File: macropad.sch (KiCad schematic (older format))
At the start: 36 parts, among them J1 USB_C_Receptacle_USB2.0, J2 TC2050-IDC, J3 CONN_LCD, U1 XC6206P332MR, U2 USBLC6-2SC6, U3 STM32F303RCTx, Y1 32MHz

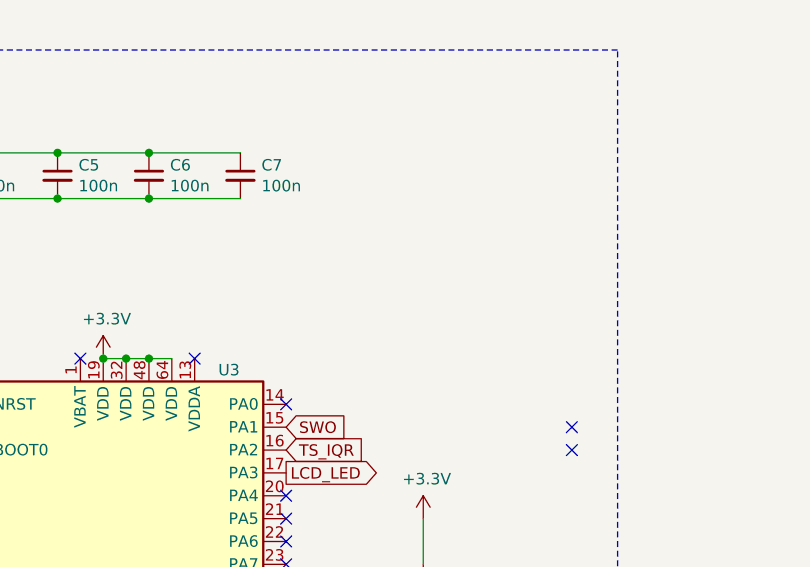
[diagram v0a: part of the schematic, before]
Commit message: Added known issues list to readme and a todo to the schematic
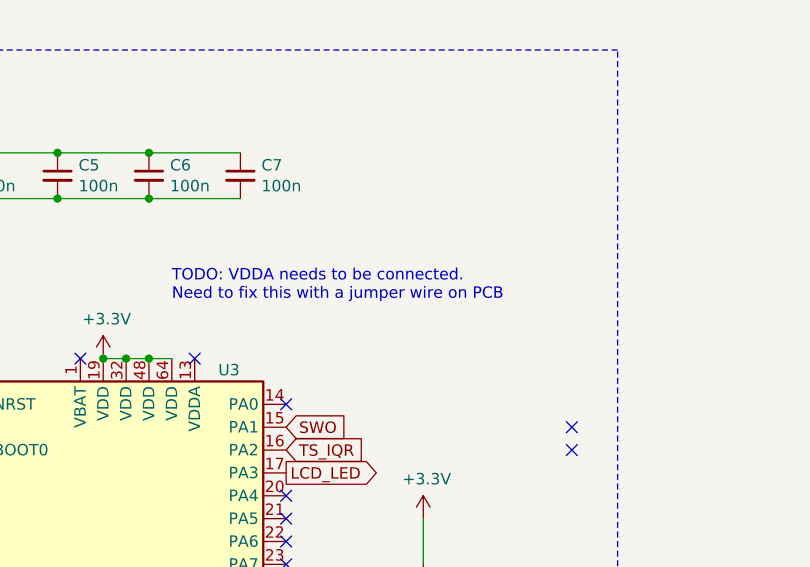
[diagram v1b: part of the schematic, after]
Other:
- note added: "TODO: VDDA needs to be connected. \nNeed to fix this with a jumper wire on PCB"
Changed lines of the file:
@@
 	1    0    0    -1
 $EndComp
+Text Notes 3600 3400 0    50   ~ 0
+TODO: VDDA needs to be connected. \nNeed to fix this with a jumper wire on PCB
 $EndSCHEMATC

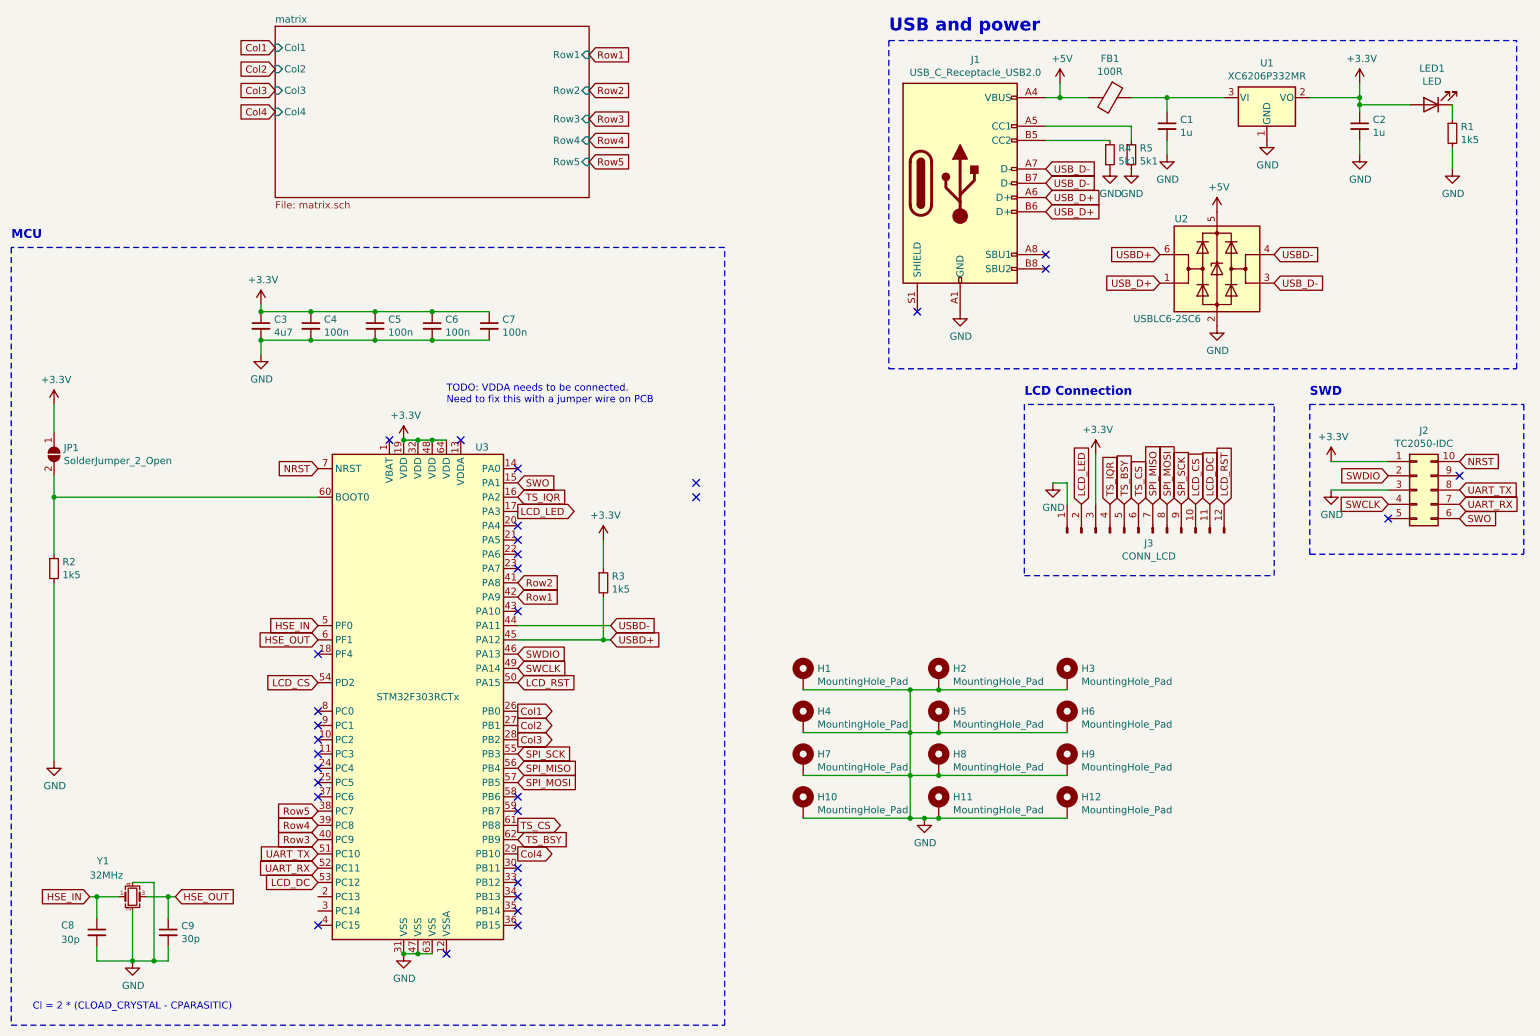
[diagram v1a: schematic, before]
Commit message: Started working on rev2 as a two-layer design
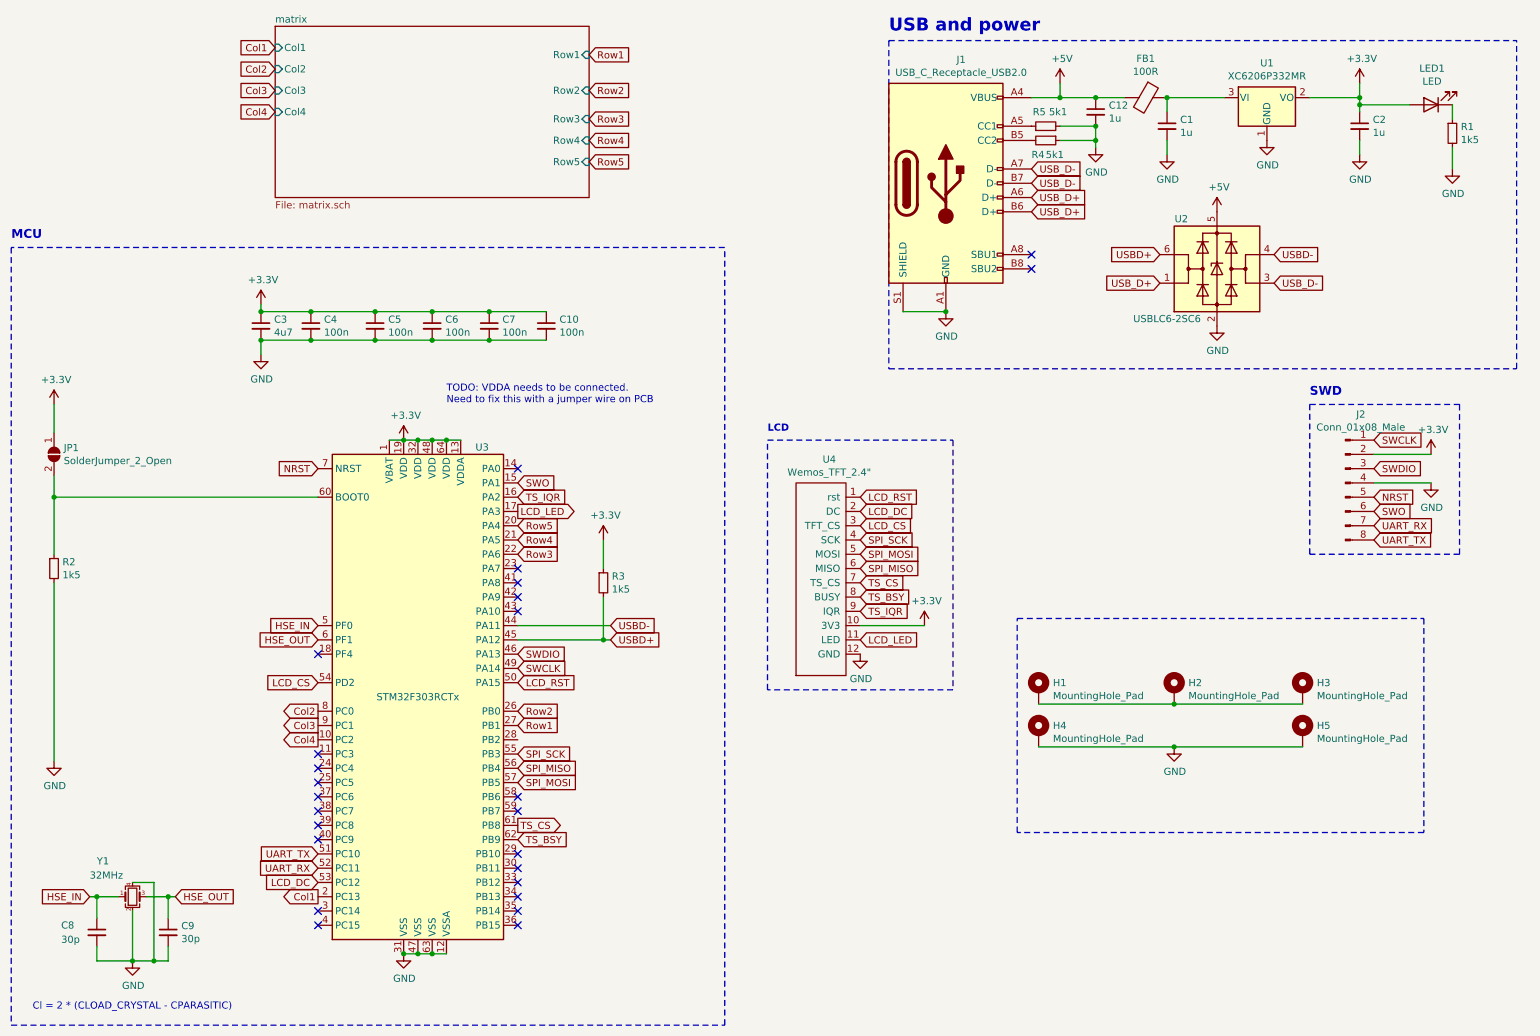
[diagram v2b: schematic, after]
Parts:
- removed H1, H2, H3, H4: MountingHole_Pad, MountingHole:MountingHole_2.2mm_M2_Pad_Via, symbol Mechanical:MountingHole_Pad
- removed H10, H11, H12: MountingHole_Pad, MountingHole:MountingHole_2.7mm_M2.5_Pad_Via, symbol Mechanical:MountingHole_Pad
- removed J2: TC2050-IDC, Connector:Tag-Connect_TC2050-IDC-FP_2x05_P1.27mm_Vertical, symbol Connector_Generic:Conn_02x05_Counter_Clockwise
- removed J3: CONN_LCD, Connector_PinHeader_2.54mm:PinHeader_1x12_P2.54mm_Vertical, symbol Connector:Conn_01x12_Male
- added C10: 100n, Capacitor_SMD:C_0603_1608Metric_Pad1.05x0.95mm_HandSolder, symbol Device:C_Small
- added C12: 1u, Capacitor_SMD:C_0603_1608Metric_Pad1.05x0.95mm_HandSolder, symbol Device:C_Small
- added J2: Conn_01x08_Male, macropad:PinHeader_1x08_P2.54mm_Vertical, symbol Connector:Conn_01x08_Male
- added U4: Wemos_TFT_2.4\", macropad:Lolin_TFT_2.4, symbol macropad:Wemos_TFT_2.4"
- renumbered H5 to H1, H6 to H2, H7 to H3, H8 to H4, H9 to H5
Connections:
- net +3V3: now also U3.1 (VBAT), U3.13 (VDDA), C10.1, J2.2 (Pin_2), U4.10 (3V3)
- net +5V: now also C12.1
- net Col1: now also U3.2 (PC13); no longer U3.26 (PB0)
- net Col2: now also U3.8 (PC0); no longer U3.27 (PB1)
- net Col3: now also U3.9 (PC1); no longer U3.28 (PB2)
- net Col4: now also U3.10 (PC2); no longer U3.29 (PB10)
- net GND: now also J1.S1 (SHIELD), R4.1, U3.12 (VSSA), C10.2, C12.2, J2.4 (Pin_4), U4.12 (GND); no longer H1.1, H2.1, H3.1, R4.2
- net LCD_CS: now also U4.3 (TFT_CS)
- net LCD_DC: now also U4.2 (DC)
- net LCD_LED: now also U4.11 (LED)
- net LCD_RST: now also U4.1 (rst)
- net NRST: now also J2.5 (Pin_5)
- net Row1: now also U3.27 (PB1); no longer U3.42 (PA9)
- net Row2: now also U3.26 (PB0); no longer U3.41 (PA8)
- net Row3: now also U3.22 (PA6); no longer U3.40 (PC9)
- net Row4: now also U3.21 (PA5); no longer U3.39 (PC8)
- net Row5: now also U3.20 (PA4); no longer U3.38 (PC7)
- net SPI_MISO: now also U4.6 (MISO)
- net SPI_MOSI: now also U4.5 (MOSI)
- net SPI_SCK: now also U4.4 (SCK)
- net SWCLK: now also J2.1 (Pin_1)
- net SWDIO: now also J2.3 (Pin_3)
- net SWO: now also J2.6 (Pin_6)
- net TS_BSY: now also U4.8 (BUSY)
- net TS_CS: now also U4.7 (TS_CS)
- net TS_IQR: now also U4.9 (IQR)
- net UART_RX: now also J2.7 (Pin_7)
- net UART_TX: now also J2.8 (Pin_8)
- net at J1.B5 (CC2): now also R4.2; no longer R4.1
- new net: H1.1, H2.1, H3.1
- no-connect marks 32 -> 25
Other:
- note added: "LCD"
- note removed: "LCD Connection"
- moved on the sheet: FB1, H1, H2, H3, H4, H5, J1, R4, R5

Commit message: Added new PCB and Schematic
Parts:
- removed C8, C9: 30p, Capacitor_SMD:C_0603_1608Metric_Pad1.05x0.95mm_HandSolder, symbol Device:C_Small
- removed H3: MountingHole_Pad, MountingHole:MountingHole_2.7mm_M2.5_Pad_Via, symbol Mechanical:MountingHole_Pad
- removed R3: 1k5, Resistor_SMD:R_0603_1608Metric_Pad1.05x0.95mm_HandSolder, symbol Device:R_Small
- removed U1: XC6206P332MR, Package_TO_SOT_SMD:SOT-23, symbol Regulator_Linear:XC6206PxxxMR
- removed U3: STM32F303RCTx, Package_QFP:LQFP-64_10x10mm_P0.5mm, symbol MCU_ST_STM32F3:STM32F303RCTx
- removed Y1: 32MHz, Crystal:Crystal_SMD_7050-4Pin_7.0x5.0mm, symbol Device:Crystal_GND24_Small
- added C14, C2, C4, C5: 10u, Capacitor_SMD:C_0603_1608Metric_Pad1.05x0.95mm_HandSolder, symbol Device:C_Small
- added C7: 4u7, Capacitor_SMD:C_0603_1608Metric_Pad1.05x0.95mm_HandSolder, symbol Device:C_Small
- added U1: AZ1117-3.3, Package_TO_SOT_SMD:SOT-223, symbol Regulator_Linear:AZ1117-3.3
- added U4: STM32F072CBTx, Package_QFP:LQFP-48_7x7mm_P0.5mm, symbol MCU_ST_STM32F0:STM32F072CBTx
- C3: renamed from C1; value 1u -> 10u
- C6: renamed from C2; value 1u -> 10u
- renumbered C12 to C1, C6 to C10, C3 to C11, C10 to C12, C7 to C13, C4 to C8, C5 to C9, H4 to H3, H5 to H4, R5 to R1, R1 to R2, R4 to R3, R2 to R4, U4 to U3
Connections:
- net +3V3: now also C14.1, C4.1, C5.1, C7.1, U1.2 (VO), U4.1 (VBAT), U4.24 (VDD), U4.36 (VDDIO2), U4.48 (VDD), U4.9 (VDDA)
- net Col1: now also U4.2 (PC13)
- net Col2: now also U4.3 (PC14)
- net Col3: now also U4.4 (PC15)
- net Col4: now also U4.5 (PF0)
- net GND: now also H1.1, H2.1, C14.2, C2.2, C4.2, C5.2, C7.2, U1.1 (GND), U4.23 (VSS), U4.35 (VSS), U4.47 (VSS), U4.8 (VSSA)
- net LCD_CS: now also U4.40 (PB4)
- net LCD_DC: now also U4.39 (PB3)
- net LCD_LED: now also U4.46 (PB9)
- net LCD_RST: now also U4.38 (PA15)
- net NRST: now also U4.7 (NRST)
- net Row1: now also U4.22 (PB11)
- net Row2: now also U4.21 (PB10)
- net Row3: now also U4.20 (PB2)
- net Row4: now also U4.19 (PB1)
- net Row5: now also U4.18 (PB0)
- net SPI_MISO: now also U4.16 (PA6)
- net SPI_MOSI: now also U4.17 (PA7)
- net SPI_SCK: now also U4.15 (PA5)
- net SWCLK: now also U4.37 (PA14)
- net SWDIO: now also U4.34 (PA13)
- net TS_BSY: now also U4.42 (PB6)
- net TS_CS: now also U4.41 (PB5)
- net TS_IQR: now also U4.45 (PB8)
- net UART_RX: now also U4.13 (PA3)
- net UART_TX: now also U4.12 (PA2)
- net USBD+: now also U2.4 (I/O2), U4.33 (PA12); no longer U2.6 (I/O1)
- net USBD-: now also U2.6 (I/O1), U4.32 (PA11); no longer U2.4 (I/O2)
- net USB_D+: now also U2.3 (I/O2); no longer U2.1 (I/O1)
- net USB_D-: now also U2.1 (I/O1); no longer U2.3 (I/O2)
- net at C3.1, FB1.1: now also C2.1, U1.3 (VI)
- net at JP1.2 (B), R4.1: now also U4.44 (BOOT0)
- net SWO: no longer names the net of J2.6 (Pin_6)
- no-connect marks 25 -> 15
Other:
- note removed: "Cl = 2 * (CLOAD_CRYSTAL - CPARASITIC)"
- note removed: "TODO: VDDA needs to be connected. \nNeed to fix this with a jumper wire on PCB"
- moved on the sheet: C10, C11, C12, C13, C8, C9, FB1, H2, U2
